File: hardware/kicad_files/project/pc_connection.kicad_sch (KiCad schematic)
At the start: 21 parts, among them U4 GT-USB-7010ASV, U5 FT232H

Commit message: feat: optimize layout, reassign annotations, add 2x4 header for UART selection
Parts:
- R13: value 10k -> 10k
- R14: value 12K -> 12K
- R16: value 150 -> 150
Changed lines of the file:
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@@
 			)
 		)
-		(property "Value" "10k "
+		(property "Value" "10k"
 			(at 144.526 72.136 90)
 			(effects
@@
 		(dnp no)
 		(fields_autoplaced yes)
-		(property "Reference" "#PWR029"
+		(property "Reference" "#PWR033"
 			(at 77.47 134.62 0)
 			(effects
@@
 			(project "FABulous_board"
 				(path "/5664f05e-a3ef-4177-8026-c4580fa32c71/b4d9b251-031a-4875-8b01-0478a187070c"
-					(reference "#PWR029")
+					(reference "#PWR033")
 					(unit 1)
 				)
@@
 		(dnp no)
 		(fields_autoplaced yes)
-		(property "Reference" "#PWR034"
+		(property "Reference" "#PWR038"
 			(at 142.24 134.62 0)
 			(effects
@@
 			(project "FABulous_board"
 				(path "/5664f05e-a3ef-4177-8026-c4580fa32c71/b4d9b251-031a-4875-8b01-0478a187070c"
-					(reference "#PWR034")
+					(reference "#PWR038")
 					(unit 1)
 				)
@@
 		(on_board yes)
 		(dnp no)
-		(property "Reference" "#PWR033"
+		(property "Reference" "#PWR037"
 			(at 142.24 69.85 0)
 			(effects
@@
 			(project "FABulous_board"
 				(path "/5664f05e-a3ef-4177-8026-c4580fa32c71/b4d9b251-031a-4875-8b01-0478a187070c"
-					(reference "#PWR033")
+					(reference "#PWR037")
 					(unit 1)
 				)
@@
 		(dnp no)
 		(fields_autoplaced yes)
-		(property "Reference" "#PWR031"
+		(property "Reference" "#PWR035"
 			(at 105.41 134.62 0)
 			(effects
@@
 			(project "FABulous_board"
 				(path "/5664f05e-a3ef-4177-8026-c4580fa32c71/b4d9b251-031a-4875-8b01-0478a187070c"
-					(reference "#PWR031")
+					(reference "#PWR035")
 					(unit 1)
 				)
@@
 		(dnp no)
 		(fields_autoplaced yes)
-		(property "Reference" "#PWR030"
+		(property "Reference" "#PWR034"
 			(at 91.44 134.62 0)
 			(effects
@@
 			(project "FABulous_board"
 				(path "/5664f05e-a3ef-4177-8026-c4580fa32c71/b4d9b251-031a-4875-8b01-0478a187070c"
-					(reference "#PWR030")
+					(reference "#PWR034")
 					(unit 1)
 				)
@@
 		(dnp no)
 		(fields_autoplaced yes)
-		(property "Reference" "#PWR032"
+		(property "Reference" "#PWR036"
 			(at 121.92 134.62 0)
 			(effects
@@
 			(project "FABulous_board"
 				(path "/5664f05e-a3ef-4177-8026-c4580fa32c71/b4d9b251-031a-4875-8b01-0478a187070c"
-					(reference "#PWR032")
+					(reference "#PWR036")
 					(unit 1)
 				)
@@
 		(dnp no)
 		(fields_autoplaced yes)
-		(property "Reference" "#PWR041"
+		(property "Reference" "#PWR045"
 			(at 252.73 77.47 0)
 			(effects
@@
 			(project "FABulous_board"
 				(path "/5664f05e-a3ef-4177-8026-c4580fa32c71/b4d9b251-031a-4875-8b01-0478a187070c"
-					(reference "#PWR041")
+					(reference "#PWR045")
 					(unit 1)
 				)
@@
 		(dnp no)
 		(fields_autoplaced yes)
-		(property "Reference" "#PWR028"
+		(property "Reference" "#PWR032"
 			(at 69.85 134.62 0)
 			(effects
@@
 			(project "FABulous_board"
 				(path "/5664f05e-a3ef-4177-8026-c4580fa32c71/b4d9b251-031a-4875-8b01-0478a187070c"
-					(reference "#PWR028")
+					(reference "#PWR032")
 					(unit 1)
 				)
@@
 		(dnp no)
 		(fields_autoplaced yes)
-		(property "Reference" "#PWR038"
+		(property "Reference" "#PWR042"
 			(at 184.15 157.48 0)
 			(effects
@@
 			(project "FABulous_board"
 				(path "/5664f05e-a3ef-4177-8026-c4580fa32c71/b4d9b251-031a-4875-8b01-0478a187070c"
-					(reference "#PWR038")
+					(reference "#PWR042")
 					(unit 1)
 				)
@@
 			)
 		)
-		(property "Value" "150 "
+		(property "Value" "150"
 			(at 264.668 82.296 90)
 			(effects
@@
 		(on_board yes)
 		(dnp no)
-		(property "Reference" "#PWR036"
+		(property "Reference" "#PWR040"
 			(at 166.37 69.85 0)
 			(effects
@@
 			(project "FABulous_board"
 				(path "/5664f05e-a3ef-4177-8026-c4580fa32c71/b4d9b251-031a-4875-8b01-0478a187070c"
-					(reference "#PWR036")
+					(reference "#PWR040")
 					(unit 1)
 				)
@@
 		(dnp no)
 		(fields_autoplaced yes)
-		(property "Reference" "#PWR037"
+		(property "Reference" "#PWR041"
 			(at 173.99 157.48 0)
 			(effects
@@
 			(project "FABulous_board"
 				(path "/5664f05e-a3ef-4177-8026-c4580fa32c71/b4d9b251-031a-4875-8b01-0478a187070c"
-					(reference "#PWR037")
+					(reference "#PWR041")
 					(unit 1)
 				)
@@
 		(dnp no)
 		(fields_autoplaced yes)
-		(property "Reference" "#PWR027"
+		(property "Reference" "#PWR031"
 			(at 64.77 134.62 0)
 			(effects
@@
 			(project "FABulous_board"
 				(path "/5664f05e-a3ef-4177-8026-c4580fa32c71/b4d9b251-031a-4875-8b01-0478a187070c"
-					(reference "#PWR027")
+					(reference "#PWR031")
 					(unit 1)
 				)
@@
 		(dnp no)
 		(fields_autoplaced yes)
-		(property "Reference" "#PWR040"
+		(property "Reference" "#PWR044"
 			(at 242.57 73.66 0)
 			(effects
@@
 			(project "FABulous_board"
 				(path "/5664f05e-a3ef-4177-8026-c4580fa32c71/b4d9b251-031a-4875-8b01-0478a187070c"
-					(reference "#PWR040")
+					(reference "#PWR044")
 					(unit 1)
 				)
@@
 		(dnp no)
 		(fields_autoplaced yes)
-		(property "Reference" "#PWR039"
+		(property "Reference" "#PWR043"
 			(at 191.77 50.8 0)
 			(effects
@@
 			(project "FABulous_board"
 				(path "/5664f05e-a3ef-4177-8026-c4580fa32c71/b4d9b251-031a-4875-8b01-0478a187070c"
-					(reference "#PWR039")
+					(reference "#PWR043")
 					(unit 1)
 				)
@@
 			)
 		)
-		(property "Value" "12K "
+		(property "Value" "12K"
 			(at 153.162 110.236 90)
 			(effects
@@
 		(dnp no)
 		(fields_autoplaced yes)
-		(property "Reference" "#PWR035"
+		(property "Reference" "#PWR039"
 			(at 149.86 134.62 0)
 			(effects
@@
 			(project "FABulous_board"
 				(path "/5664f05e-a3ef-4177-8026-c4580fa32c71/b4d9b251-031a-4875-8b01-0478a187070c"
-					(reference "#PWR035")
+					(reference "#PWR039")
 					(unit 1)
 				)
@@
 		(dnp no)
 		(fields_autoplaced yes)
-		(property "Reference" "#PWR042"
+		(property "Reference" "#PWR046"
 			(at 261.62 77.47 0)
 			(effects
@@
 			(project "FABulous_board"
 				(path "/5664f05e-a3ef-4177-8026-c4580fa32c71/b4d9b251-031a-4875-8b01-0478a187070c"
-					(reference "#PWR042")
+					(reference "#PWR046")
 					(unit 1)
 				)
@@
 		(dnp no)
 		(fields_autoplaced yes)
-		(property "Reference" "#PWR026"
+		(property "Reference" "#PWR030"
 			(at 31.75 133.35 0)
 			(effects
@@
 			(project "FABulous_board"
 				(path "/5664f05e-a3ef-4177-8026-c4580fa32c71/b4d9b251-031a-4875-8b01-0478a187070c"
-					(reference "#PWR026")
-					(unit 1)
-				)
+					(reference "#PWR030")
+					(unit 1)
+				)

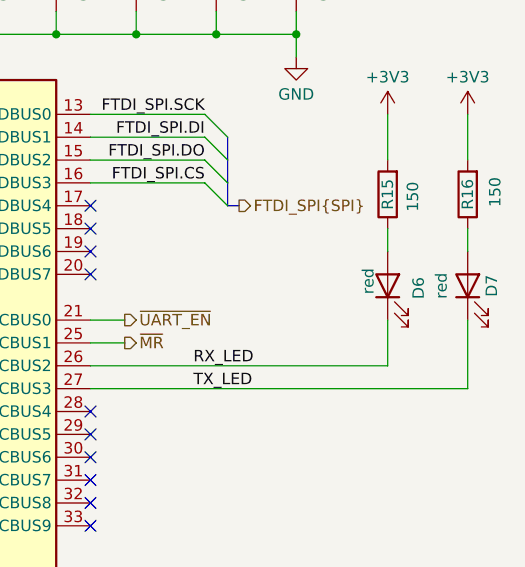
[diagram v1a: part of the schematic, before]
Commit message: feat: implemented all suggestions, logos still missing or incorrect
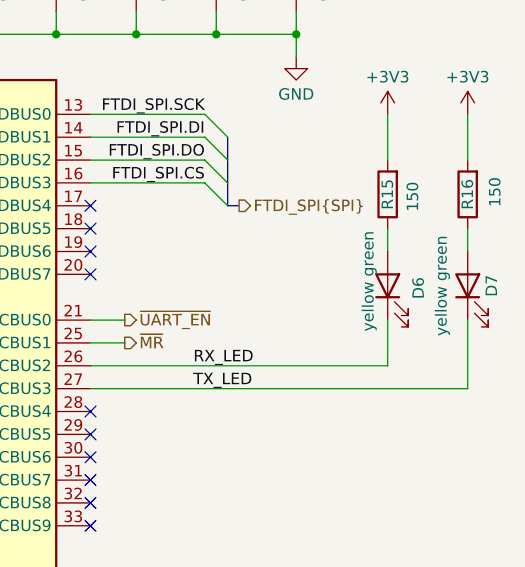
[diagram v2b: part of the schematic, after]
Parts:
- D6, D7: value red -> yellow green; LCSC Number (none) -> C7496846
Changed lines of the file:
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@@
 			)
 		)
-		(property "Value" "red"
+		(property "Value" "yellow green"
 			(at 250.571 92.202 0)
 			(effects
@@
 		)
 		(property "Description" "Light emitting diode"
+			(at 252.73 92.71 0)
+			(effects
+				(font
+					(size 1.27 1.27)
+				)
+				(hide yes)
+			)
+		)
+		(property "LCSC Number" "C7496846"
 			(at 252.73 92.71 0)
 			(effects
@@
 			)
 		)
-		(property "Value" "red"
+		(property "Value" "yellow green"
 			(at 258.699 92.71 0)
 			(effects
@@
 			(at 261.62 92.71 0)
 			(effects
+				(font
+					(size 1.27 1.27)
+				)
+				(hide yes)
+			)
+		)
+		(property "LCSC Number" "C7496846"
+			(at 261.62 92.71 0)
+			(effects

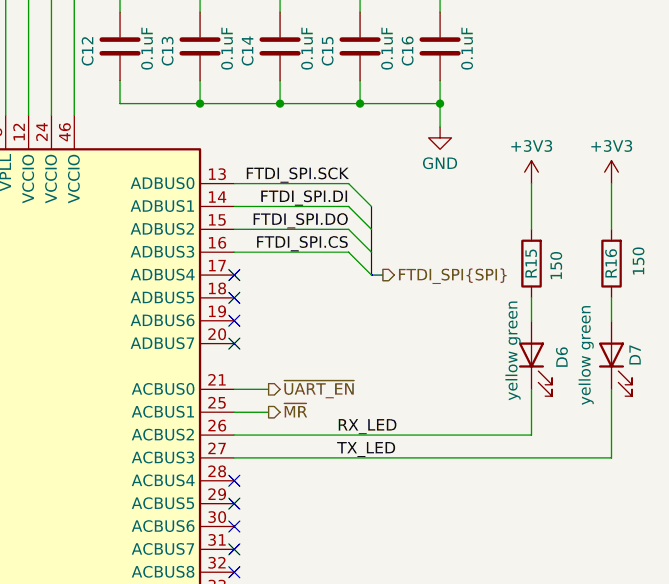
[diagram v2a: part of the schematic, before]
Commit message: feat: Implement all findings of the second review
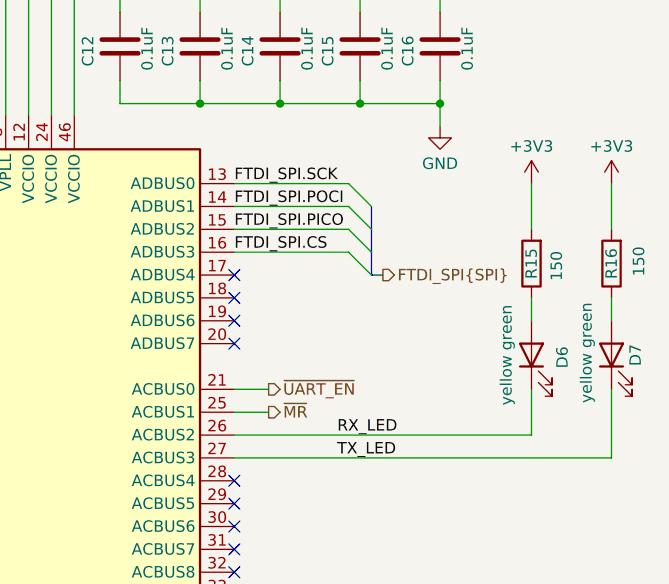
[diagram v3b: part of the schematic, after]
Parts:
- D6, D7: value yellow green -> C965826; LCSC Number C7496846 -> C965826
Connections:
- net FTDI_SPI.DI renamed FTDI_SPI.POCI
- net FTDI_SPI.DO renamed FTDI_SPI.PICO
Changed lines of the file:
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@@
+	(wire
+		(pts
+			(xy 219.71 73.66) (xy 232.41 73.66)
+		)
+		(stroke
+			(width 0)
+			(type default)
+		)
+	)
 	(wire
 		(pts
@@
 	(wire
 		(pts
-			(xy 232.41 81.28) (xy 219.71 81.28)
-		)
-		(stroke
-			(width 0)
-			(type default)
-		)
-	)
-	(wire
-		(pts
 			(xy 242.57 52.07) (xy 242.57 54.61)
 		)
@@
 	(wire
 		(pts
-			(xy 232.41 76.2) (xy 219.71 76.2)
-		)
-		(stroke
-			(width 0)
-			(type default)
-		)
-	)
-	(wire
-		(pts
 			(xy 184.15 148.59) (xy 186.69 148.59)
 		)
@@
 	(wire
 		(pts
+			(xy 219.71 76.2) (xy 232.41 76.2)
+		)
+		(stroke
+			(width 0)
+			(type default)
+		)
+	)
+	(wire
+		(pts
 			(xy 171.45 123.19) (xy 171.45 127)
 		)
@@
 	(wire
 		(pts
+			(xy 219.71 78.74) (xy 232.41 78.74)
+		)
+		(stroke
+			(width 0)
+			(type default)
+		)
+	)
+	(wire
+		(pts
 			(xy 261.62 73.66) (xy 261.62 78.74)
 		)
@@
 	(wire
 		(pts
+			(xy 219.71 81.28) (xy 232.41 81.28)
+		)
+		(stroke
+			(width 0)
+			(type default)
+		)
+	)
+	(wire
+		(pts
 			(xy 196.85 148.59) (xy 199.39 148.59)
 		)
@@
 	(wire
 		(pts
-			(xy 232.41 78.74) (xy 219.71 78.74)
-		)
-		(stroke
-			(width 0)
-			(type default)
-		)
-	)
-	(wire
-		(pts
 			(xy 233.68 52.07) (xy 242.57 52.07)
 		)
@@
 		(pts
 			(xy 77.47 110.49) (xy 77.47 128.27)
-		)
-		(stroke
-			(width 0)
-			(type default)
-		)
-	)
-	(wire
-		(pts
-			(xy 232.41 73.66) (xy 219.71 73.66)
 		)
 		(stroke
@@
 	)
 	(label "FTDI_SPI.SCK"
-		(at 232.41 73.66 180)
+		(at 219.71 73.66 0)
 		(fields_autoplaced yes)
 		(effects
@@
 				(size 1.27 1.27)
 			)
-			(justify right bottom)
-		)
-	)
-	(label "FTDI_SPI.DI"
-		(at 232.41 76.2 180)
+			(justify left bottom)
+		)
+	)
+	(label "FTDI_SPI.POCI"
+		(at 219.71 76.2 0)
 		(fields_autoplaced yes)
 		(effects
@@
 				(size 1.27 1.27)
 			)
-			(justify right bottom)
+			(justify left bottom)
 		)
 	)
@@
 	)
 	(label "FTDI_SPI.CS"
-		(at 232.41 81.28 180)
+		(at 219.71 81.28 0)
 		(fields_autoplaced yes)
 		(effects
@@
 				(size 1.27 1.27)
 			)
-			(justify right bottom)
+			(justify left bottom)
 		)
 	)
@@
 		)
 	)
-	(label "FTDI_SPI.DO"
-		(at 232.41 78.74 180)
+	(label "FTDI_SPI.PICO"
+		(at 219.71 78.74 0)
 		(fields_autoplaced yes)
 		(effects
@@
 				(size 1.27 1.27)
 			)
-			(justify right bottom)
+			(justify left bottom)
 		)
 	)
@@
 			)
 		)
-		(property "Value" "yellow green"
+		(property "Value" "C965826"
 			(at 250.571 92.202 0)
 			(effects
@@
 					(size 1.27 1.27)
 				)
+				(hide yes)
 			)
 		)
@@
 			)
 		)
-		(property "Description" "Light emitting diode"
-			(at 252.73 92.71 0)
-			(effects
-				(font
-					(size 1.27 1.27)
-				)
-				(hide yes)
-			)
-		)
-		(property "LCSC Number" "C7496846"
+		(property "Description" "yellow green"
+			(at 249.936 92.71 0)
+			(effects
+				(font
+					(size 1.27 1.27)
+				)
+			)
+		)
+		(property "LCSC Number" " C965826"
 			(at 252.73 92.71 0)
 			(effects
@@
 			)
 		)
-		(property "Value" "yellow green"
+		(property "Value" "C965826"
 			(at 258.699 92.71 0)
 			(effects
@@
 					(size 1.27 1.27)
 				)
+				(hide yes)
 			)
 		)
@@
 			)
 		)
-		(property "Description" "Light emitting diode"
+		(property "Description" "yellow green"
+			(at 258.826 92.456 0)
+			(effects
+				(font
+					(size 1.27 1.27)
+				)
+			)
+		)
+		(property "LCSC Number" " C965826"
 			(at 261.62 92.71 0)
 			(effects
-				(font
-					(size 1.27 1.27)
-				)
-				(hide yes)
-			)
-		)
-		(property "LCSC Number" "C7496846"
-			(at 261.62 92.71 0)
-			(effects

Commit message: fix: add offset for JLCPCB manufacturing
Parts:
- U4: JLCPCB Position Offset (none) -> 0,1.05
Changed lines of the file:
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@@
+			)
+		)
+		(property "JLCPCB Position Offset" "0,1.05"
+			(at 45.72 91.44 0)
+			(effects
+				(font
+					(size 1.27 1.27)
+				)
+				(hide yes)
 			)
 		)

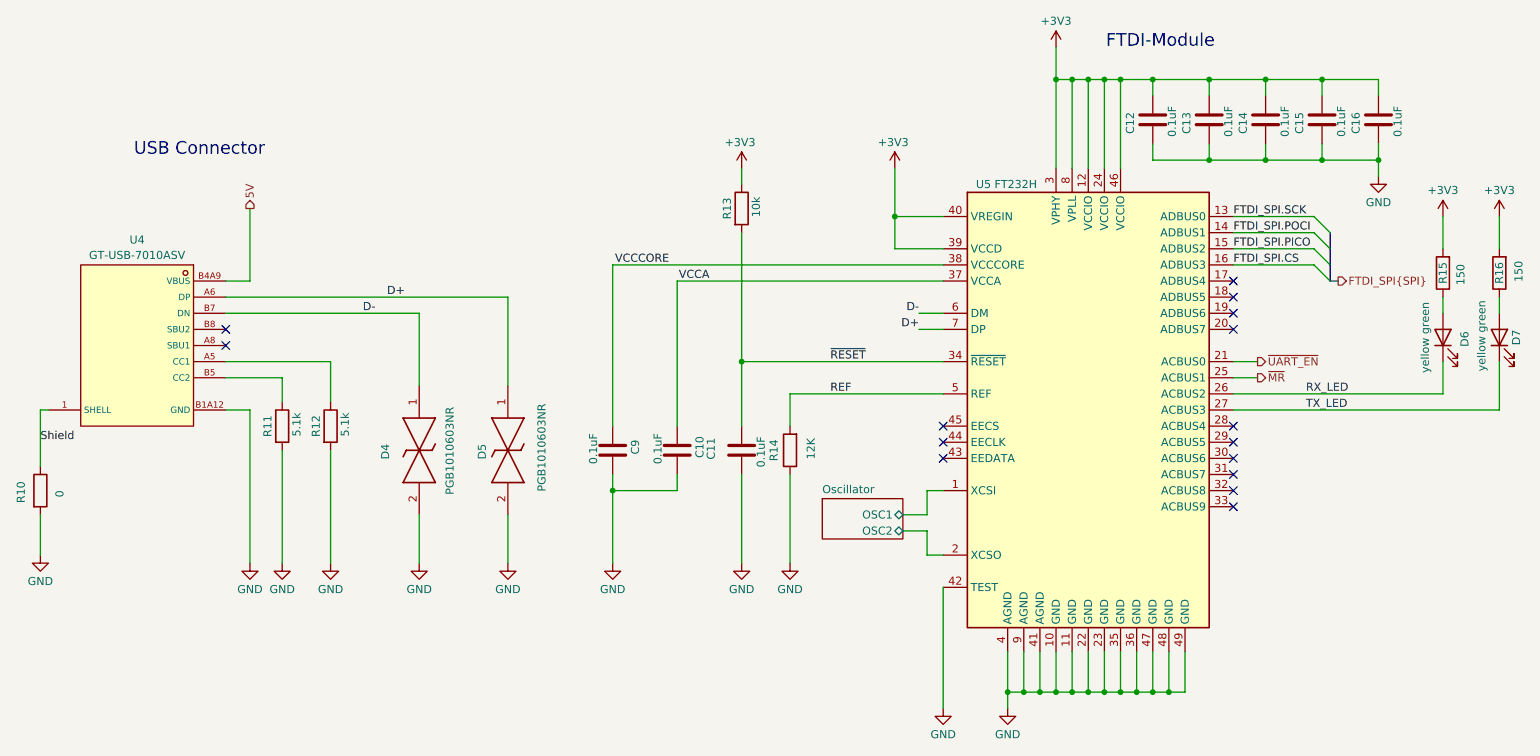
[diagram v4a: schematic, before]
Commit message: fix: replace all local symbols and footprints with versions from KiCad or project libraries
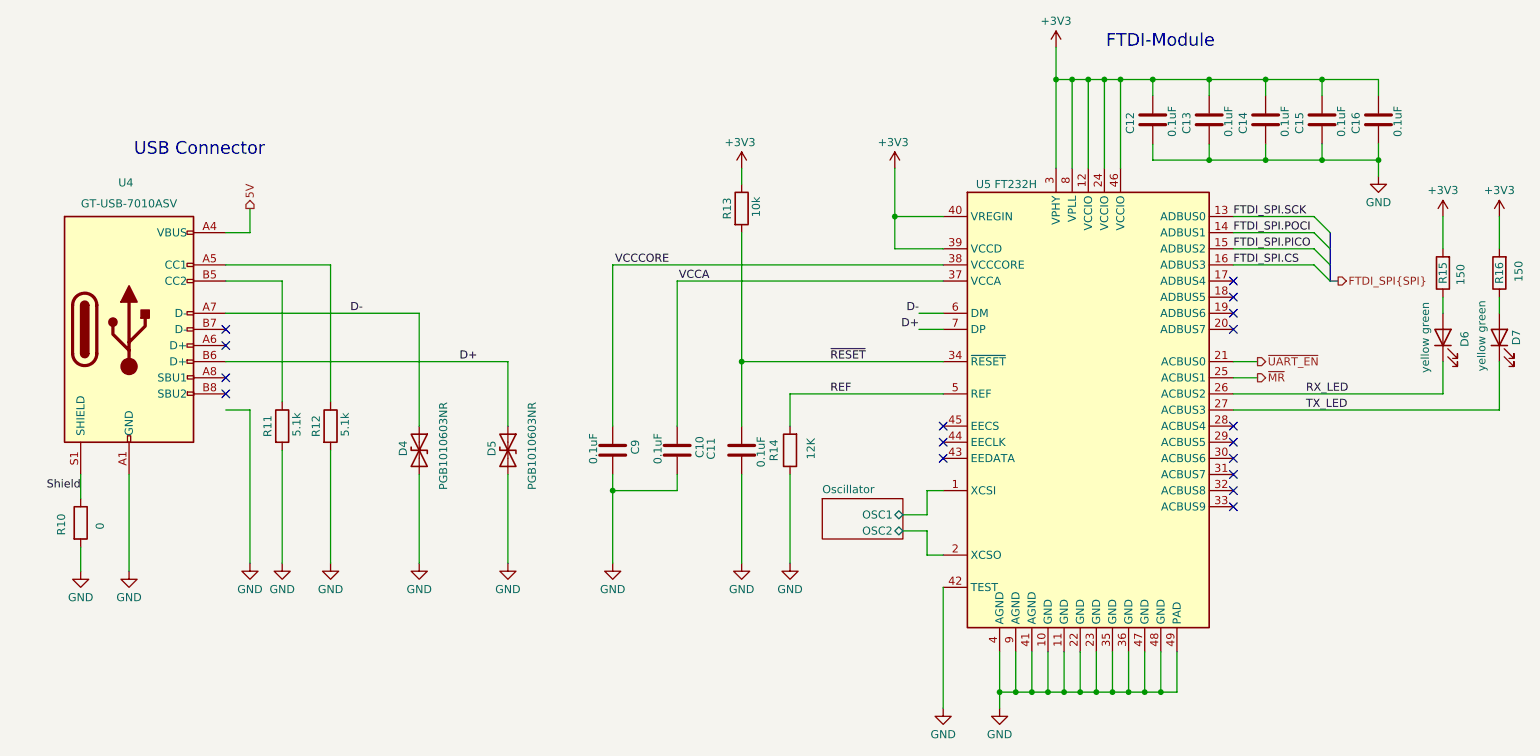
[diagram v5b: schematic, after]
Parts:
- D4: footprint easy_eda:D0603-BI -> Diode_SMD:D_0603_1608Metric; symbol PGB1010603NR:PGB1010603NR -> Device:D_TVS
- D5: footprint easy_eda:D0603-BI -> Capacitor_SMD:C_0603_1608Metric; symbol PGB1010603NR:PGB1010603NR -> Device:D_TVS
- U4: footprint easy_eda:USB-C-SMD_G-SWITCH_GT-USB-7010ASV -> Customized:USB_C_Receptacle_GCT_USB4105-xx-A_16P_TopMnt_Horizontal; symbol easy_eda:GT-USB-7010ASV -> custom_symbols:USB_C_Receptacle_USB2.0_14P
- U5: symbol FABulous:FT232H -> custom_symbols:FT232H_PAD_GND
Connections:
- net 5V: now also U4.A4 (VBUS), U4.A9 (VBUS); no longer U4.A4B9 (VBUS), U4.B4A9 (VBUS)
- net D+: no longer U4.A6 (DP)
- net D-: no longer U4.B7 (DN)
- net GND: now also U4.A1 (GND), U4.A12 (GND); no longer U4.A1B12 (GND), U4.B1A12 (GND)
- net Shield: now also U4.S1 (SHIELD); no longer U4.1 (SHELL), U4.2 (SHELL), U4.3 (SHELL), U4.4 (SHELL)
- no-connect marks 15 -> 17
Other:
- moved on the sheet: R10
